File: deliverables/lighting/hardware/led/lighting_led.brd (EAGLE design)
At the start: 43.2 x 62.3 mm, 17 parts, among them J1 5055780671, J2 5055780671

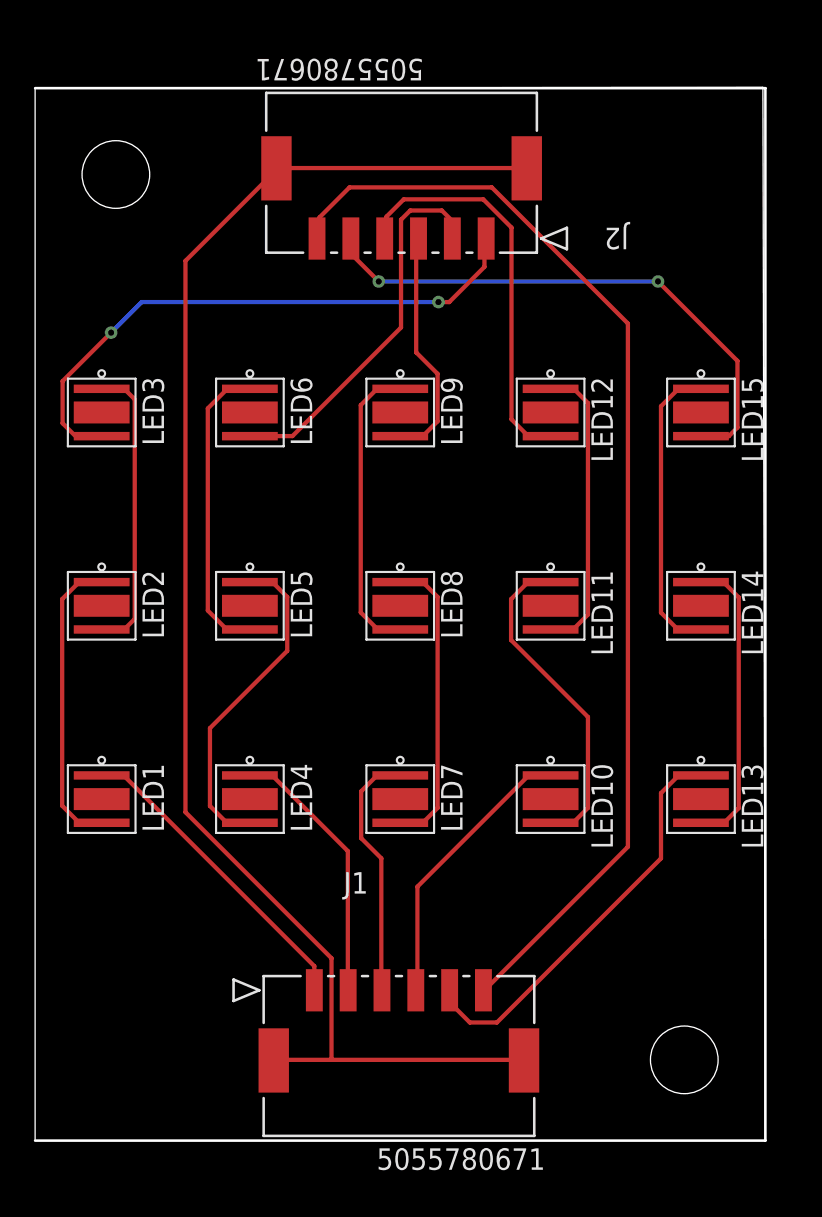
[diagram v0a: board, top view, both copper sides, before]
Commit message: Added Supporting Files for V0.2
SCH, BRD, and PNG for both
Also FBX models
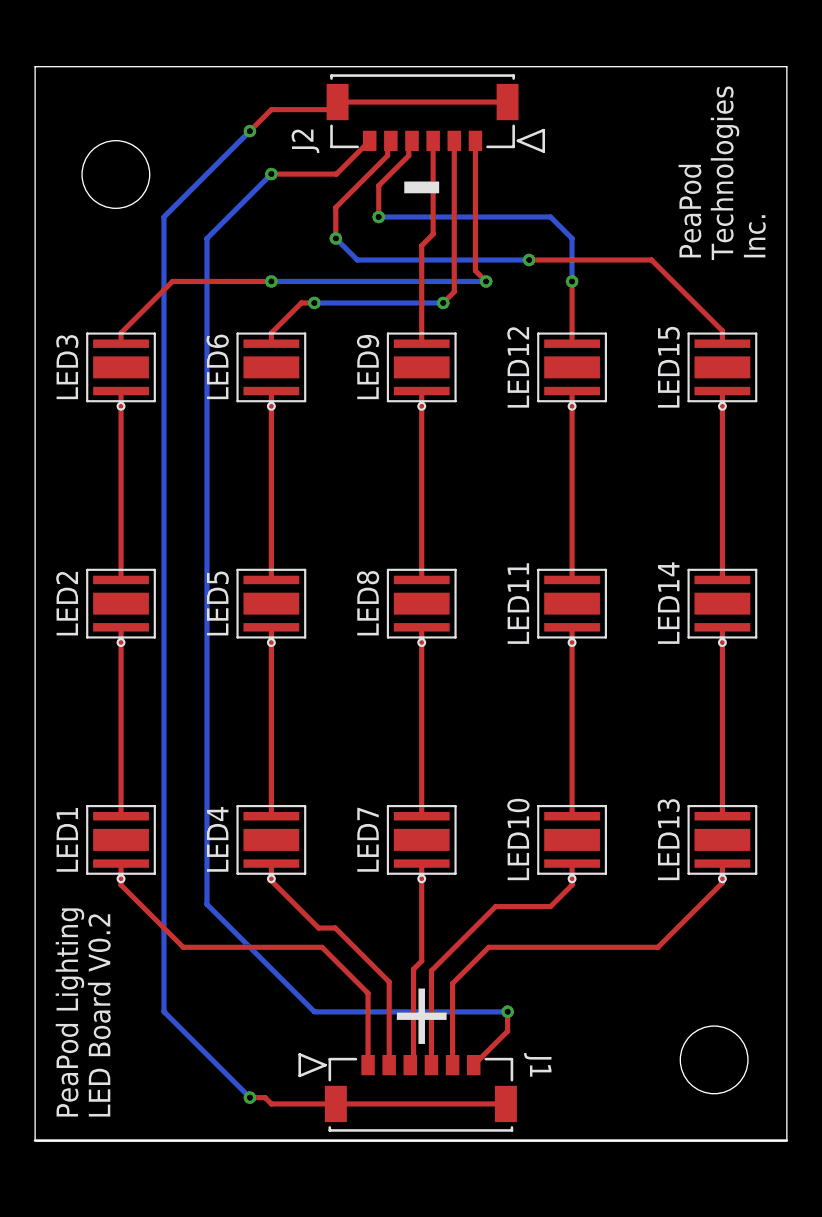
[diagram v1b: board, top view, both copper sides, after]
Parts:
- J1, J2: value 5055780671 -> MOLEX-MICROLOCK-6PIN; device Molex Micro-Lock PLUS 6-pin (90deg):CON_5055780671 -> Molex Micro-Lock PLUS 6-Pin 90deg:CON_5055670671
- LED1, LED2, LED3: value XLAMP_XP-G3_ROYAL -> XP-G3_BLUE; device XLAMP XP-G3 Royal Blue:XLAMP_XP-G3 -> XLAMP XP-G3:XLAMP_XP-G3_BLUE
- LED10, LED11, LED12: value XLAMP_XP-G3_PHOTO -> XP-G3_RED; device XLAMP XP-G3 Photo Red:XLAMP_XP-G3 -> XLAMP XP-G3:XLAMP_XP-G3_RED
- LED13, LED14, LED15: device XLAMP XP-E2 Far Red:XLAMP_XP-E2 -> Cree XLAMP XP-E2:XLAMP_XP-E2
- LED4, LED5, LED6: value XLAMP_XP-G3_COOL -> XP-G3_COOL; device XLAMP XP-G3 Cool White:XLAMP_XP-G3 -> XLAMP XP-G3:XLAMP_XP-G3_COOL
- LED7, LED8, LED9: value XLAMP_XP-G3_WARM -> XP-G3_WARM; device XLAMP XP-G3 Warm White:XLAMP_XP-G3 -> XLAMP XP-G3:XLAMP_XP-G3_WARM
- moved J2 5.81 mm to (24.8, 61.7), turned to 0 degrees
- moved J1 5.45 mm to (18.4, 7.00), turned to 180 degrees
- moved LED12 2.95 mm to (30.5, 48.3), turned to 90 degrees
- moved LED6 2.95 mm to (12.7, 48.3), turned to 90 degrees
- moved LED9 2.95 mm to (21.6, 48.3), turned to 90 degrees
- moved LED15 2.95 mm to (39.4, 48.3), turned to 90 degrees
- moved LED3 2.90 mm to (3.81, 48.3), turned to 90 degrees
- moved LED10 2.73 mm to (30.5, 20.3), turned to 90 degrees
- moved LED4 2.73 mm to (12.7, 20.3), turned to 90 degrees
- moved LED7 2.73 mm to (21.6, 20.3), turned to 90 degrees
- moved LED13 2.73 mm to (39.4, 20.3), turned to 90 degrees
- moved LED1 2.67 mm to (3.81, 20.3), turned to 90 degrees
- moved LED11 1.28 mm to (30.5, 34.3), turned to 90 degrees
- moved LED5 1.28 mm to (12.7, 34.3), turned to 90 degrees
- moved LED8 1.28 mm to (21.6, 34.3), turned to 90 degrees
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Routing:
- net N$16: track 66.6 -> 75.8 mm, vias 0 -> 2
- net N$1: track 19.6 -> 11.2 mm
- net N$7: track 19.5 -> 11.2 mm
- net N$4: track 17.9 -> 11.2 mm
- net N$10: track 17.8 -> 11.2 mm
- net N$6: track 17.7 -> 11.2 mm
- net N$2: track 17.7 -> 11.2 mm
- net N$9: track 17.7 -> 11.2 mm
- net N$8: track 17.6 -> 11.2 mm
- net N$5: track 17.6 -> 11.2 mm
- net N$3: track 17.4 -> 11.2 mm
- net N$17: track 88.1 -> 92.6 mm, vias 0 -> 2
- net N$11: track 18.7 -> 22.8 mm
- net N$13: track 15.0 -> 12.2 mm
- net N$22: track 34.7 -> 32.1 mm
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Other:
- board size 43.2 x 62.3 mm -> 44.5 x 63.5 mm
- board text added: "+"
- board text added: "-"
- board text added: "PeaPod Lighting LED Board V0.2"
- board text added: "PeaPod Technologies Inc."
